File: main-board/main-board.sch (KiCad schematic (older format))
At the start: 114 parts, among them J1 BOOT, J10 8P8CDouble, J11 Qwiic, J12 Qwiic, J13 Qwiic, J14 YELLOW, J15 GREEN, J2 USB Header, J3 JTAG, J5 StatusPanel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

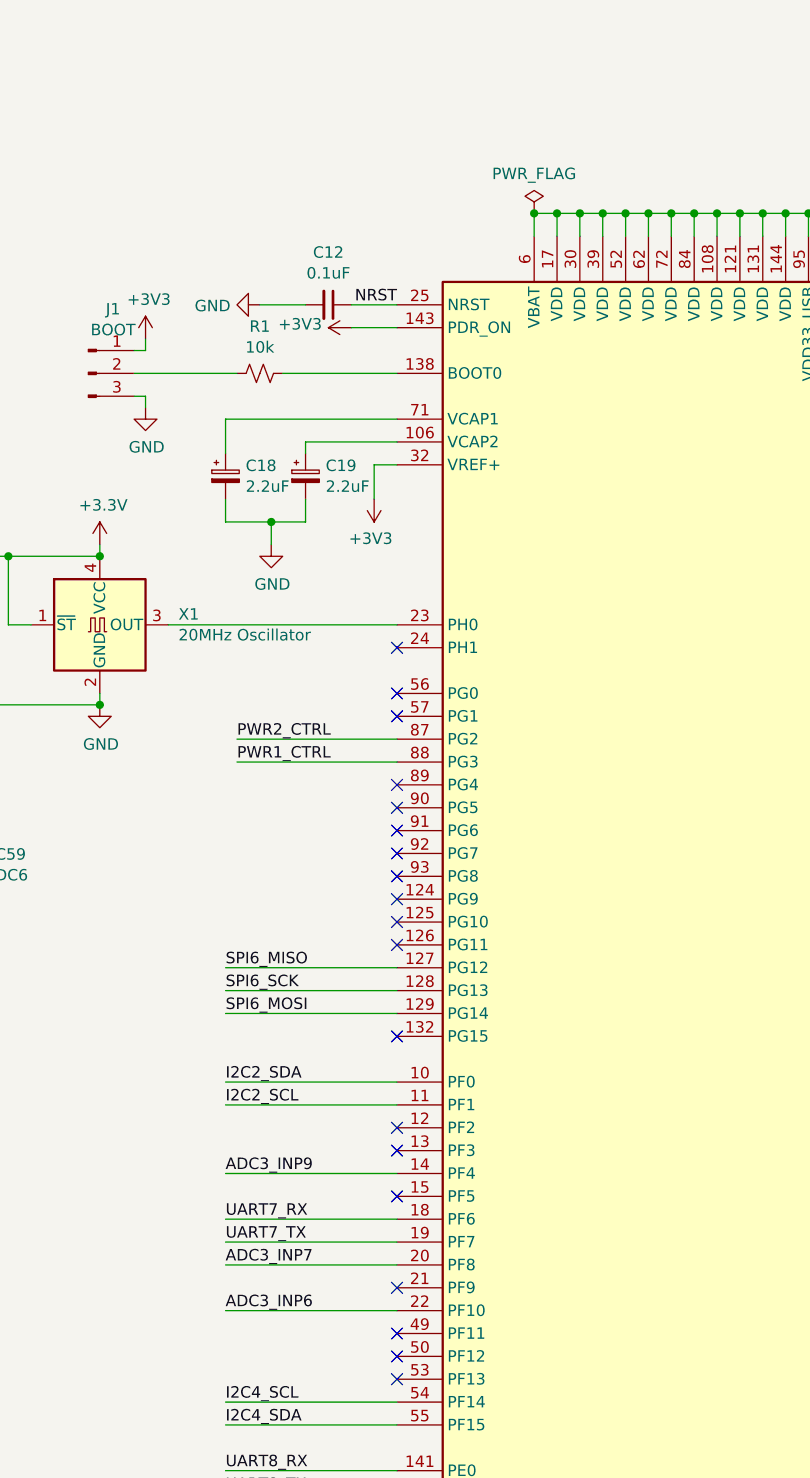
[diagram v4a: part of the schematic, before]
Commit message: Removed some unused nets and marked the pins NC
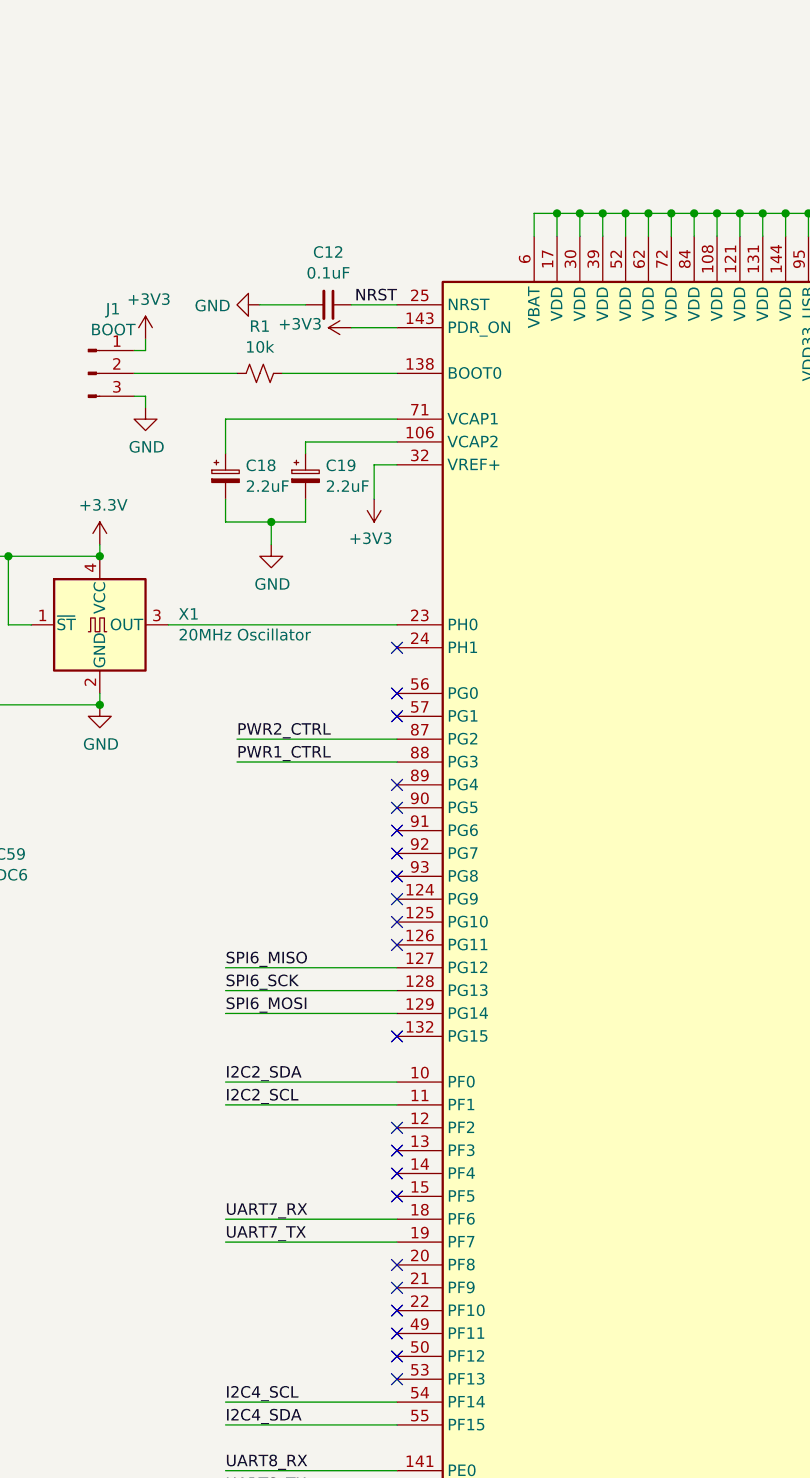
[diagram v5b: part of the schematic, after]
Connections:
- net ADC3_INP6: no longer names the net of U1.22 (PF10)
- net ADC3_INP7: no longer names the net of U1.20 (PF8)
- net ADC3_INP9: no longer names the net of U1.14 (PF4)
- no-connect marks 54 -> 57
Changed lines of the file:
@@
 USART1_RX
 Wire Wire Line
-	10650 6900 9900 6900
-Wire Wire Line
 	10650 7100 9900 7100
 Wire Wire Line
 	10650 7200 9900 7200
 Wire Wire Line
-	10650 7300 9900 7300
-Wire Wire Line
-	10650 7500 9900 7500
-Wire Wire Line
 	13150 6600 13850 6600
 Wire Wire Line
@@
 Text Label 13850 6600 2    50   ~ 0
 ETH_MDC
-Text Label 9900 6900 0    50   ~ 0
-ADC3_INP9
 Text Label 9900 7100 0    50   ~ 0
 UART7_RX
 Text Label 9900 7200 0    50   ~ 0
 UART7_TX
-Text Label 9900 7300 0    50   ~ 0
-ADC3_INP7
-Text Label 9900 7500 0    50   ~ 0
-ADC3_INP6
 Text Label 13900 3200 2    50   ~ 0
 ETH_RX_CLK
@@
 Connection ~ 12550 2700
 $Comp
-L power:PWR_FLAG #FLG0101
-U 1 1 628B99AF
-P 11250 2700
-F 0 "#FLG0101" H 11250 2775 50  0001 C CNN
-F 1 "PWR_FLAG" H 11250 2873 50  0000 C CNN
-F 2 "" H 11250 2700 50  0001 C CNN
-F 3 "~" H 11250 2700 50  0001 C CNN
-	1    11250 2700
-	1    0    0    -1
-$EndComp
-Connection ~ 11250 2700
-$Comp
 L ISL83490:ISL83490 U12
 U 1 1 62B08550
@@
 	1    0    0    -1
 $EndComp
+NoConn ~ 10650 7300
+NoConn ~ 10650 7500
+NoConn ~ 10650 6900
 $EndSCHEMATC

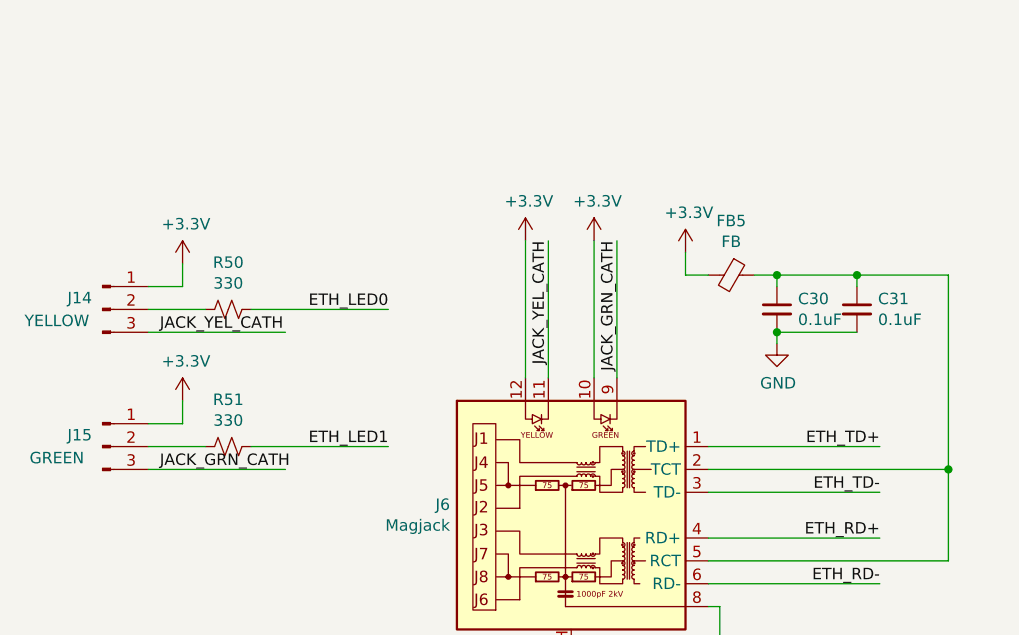
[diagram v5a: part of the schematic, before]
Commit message: Moved ethernet LEDs to a single 2x3 header instead of two 1x3
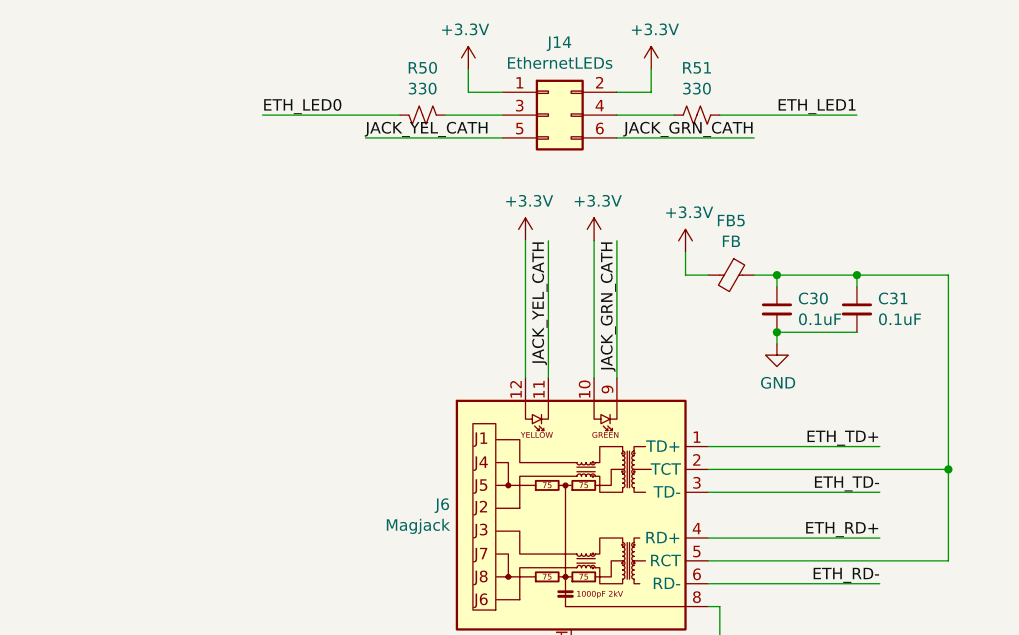
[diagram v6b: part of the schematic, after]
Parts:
- removed J14: YELLOW, Pin_Headers:Pin_Header_Straight_1x03_Pitch2.54mm, symbol Connector:Conn_01x03_Male
- removed J15: GREEN, Pin_Headers:Pin_Header_Straight_1x03_Pitch2.54mm, symbol Connector:Conn_01x03_Male
- added J14: EthernetLEDs, Pin_Headers:Pin_Header_Straight_2x03_Pitch2.54mm, symbol Connector_Generic:Conn_02x03_Odd_Even
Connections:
- net +3V3: now also J14.1 (Pin_1), J14.2 (Pin_2)
- net JACK_GRN_CATH: now also J14.6 (Pin_6)
- net JACK_YEL_CATH: now also J14.5 (Pin_5)
- net at R50.2: now also J14.3 (Pin_3)
- net at R51.2: now also J14.4 (Pin_4)
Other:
- moved on the sheet: R50, R51
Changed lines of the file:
@@
 JACK_GRN_CATH
-$Comp
-L Connector:Conn_01x03_Male J14
-U 1 1 602D7895
-P 850 1900
-F 0 "J14" H 750 1950 50  0000 C CNN
-F 1 "YELLOW" H 650 1850 50  0000 C CNN
-F 2 "Pin_Headers:Pin_Header_Straight_1x03_Pitch2.54mm" H 850 1900 50  0001 C CNN
-F 3 "~" H 850 1900 50  0001 C CNN
-	1    850  1900
-	1    0    0    -1
-$EndComp
-$Comp
-L Connector:Conn_01x03_Male J15
-U 1 1 602D90A8
-P 850 2500
-F 0 "J15" H 750 2550 50  0000 C CNN
-F 1 "GREEN" H 650 2450 50  0000 C CNN
-F 2 "Pin_Headers:Pin_Header_Straight_1x03_Pitch2.54mm" H 850 2500 50  0001 C CNN
-F 3 "~" H 850 2500 50  0001 C CNN
-	1    850  2500
-	1    0    0    -1
-$EndComp
 $Comp
 L power:+3.3V #PWR0187
 U 1 1 605E2E74
-P 1200 1700
-F 0 "#PWR0187" H 1200 1550 50  0001 C CNN
-F 1 "+3.3V" H 1215 1873 50  0000 C CNN
-F 2 "" H 1200 1700 50  0001 C CNN
-F 3 "" H 1200 1700 50  0001 C CNN
-	1    1200 1700
-	1    0    0    -1
+P 2450 850
+F 0 "#PWR0187" H 2450 700 50  0001 C CNN
+F 1 "+3.3V" H 2465 1023 50  0000 C CNN
+F 2 "" H 2450 850 50  0001 C CNN
+F 3 "" H 2450 850 50  0001 C CNN
+	1    2450 850
+	-1   0    0    -1
 $EndComp
 $Comp
@@
 $EndComp
 Wire Wire Line
-	1200 1700 1200 1800
-Wire Wire Line
-	1200 1800 1050 1800
-Wire Wire Line
-	1050 2000 1650 2000
-Text Label 1100 2000 0    50   ~ 0
+	2450 850  2450 950
+Wire Wire Line
+	2450 950  2600 950
+Wire Wire Line
+	2600 1150 2000 1150
+Text Label 2000 1150 0    50   ~ 0
 JACK_YEL_CATH
 Wire Wire Line
@@
 ETH_LED1
 Wire Wire Line
-	1050 2600 1650 2600
-Text Label 1100 2600 0    50   ~ 0
+	3100 1150 3700 1150
+Text Label 3700 1150 2    50   ~ 0
 JACK_GRN_CATH
 $Comp
 L power:+3.3V #PWR0190
 U 1 1 60BEFA4D
-P 1200 2300
-F 0 "#PWR0190" H 1200 2150 50  0001 C CNN
-F 1 "+3.3V" H 1215 2473 50  0000 C CNN
-F 2 "" H 1200 2300 50  0001 C CNN
-F 3 "" H 1200 2300 50  0001 C CNN
-	1    1200 2300
-	1    0    0    -1
-$EndComp
-Wire Wire Line
-	1200 2300 1200 2400
-Wire Wire Line
-	1200 2400 1050 2400
-Wire Wire Line
-	1500 2500 2100 2500
-Wire Wire Line
-	1500 1900 2100 1900
-Text Label 2100 1900 2    50   ~ 0
+P 3250 850
+F 0 "#PWR0190" H 3250 700 50  0001 C CNN
+F 1 "+3.3V" H 3265 1023 50  0000 C CNN
+F 2 "" H 3250 850 50  0001 C CNN
+F 3 "" H 3250 850 50  0001 C CNN
+	1    3250 850
+	1    0    0    -1
+$EndComp
+Wire Wire Line
+	3250 850  3250 950
+Wire Wire Line
+	3250 950  3100 950
+Wire Wire Line
+	3550 1050 4150 1050
+Wire Wire Line
+	2150 1050 1550 1050
+Text Label 1550 1050 0    50   ~ 0
 ETH_LED0
-Text Label 2100 2500 2    50   ~ 0
+Text Label 4150 1050 2    50   ~ 0
 ETH_LED1
 $Comp
 L Device:R_Small_US R50
 U 1 1 60F9F1DF
-P 1400 1900
-F 0 "R50" V 1195 1900 50  0000 C CNN
-F 1 "330" V 1286 1900 50  0000 C CNN
-F 2 "Resistors_SMD:R_0805" H 1400 1900 50  0001 C CNN
-F 3 "~" H 1400 1900 50  0001 C CNN
-	1    1400 1900
-	0    1    1    0
+P 2250 1050
+F 0 "R50" V 2045 1050 50  0000 C CNN
+F 1 "330" V 2136 1050 50  0000 C CNN
+F 2 "Resistors_SMD:R_0805" H 2250 1050 50  0001 C CNN
+F 3 "~" H 2250 1050 50  0001 C CNN
+	1    2250 1050
+	0    -1   1    0
 $EndComp
 $Comp
 L Device:R_Small_US R51
 U 1 1 60FA0ADB
-P 1400 2500
-F 0 "R51" V 1195 2500 50  0000 C CNN
-F 1 "330" V 1286 2500 50  0000 C CNN
-F 2 "Resistors_SMD:R_0805" H 1400 2500 50  0001 C CNN
-F 3 "~" H 1400 2500 50  0001 C CNN
-	1    1400 2500
+P 3450 1050
+F 0 "R51" V 3245 1050 50  0000 C CNN
+F 1 "330" V 3336 1050 50  0000 C CNN
+F 2 "Resistors_SMD:R_0805" H 3450 1050 50  0001 C CNN
+F 3 "~" H 3450 1050 50  0001 C CNN
+	1    3450 1050
 	0    1    1    0
 $EndComp
 Wire Wire Line
-	1050 1900 1300 1900
-Wire Wire Line
-	1050 2500 1300 2500
+	2600 1050 2350 1050
+Wire Wire Line
+	3100 1050 3350 1050
 Wire Wire Line
 	13150 9200 13850 9200
@@
 NoConn ~ 10650 7500
 NoConn ~ 10650 6900
+$Comp
+L Connector_Generic:Conn_02x03_Odd_Even J14
+U 1 1 61F985B2
+P 2800 1050
+F 0 "J14" H 2850 1367 50  0000 C CNN
+F 1 "EthernetLEDs" H 2850 1276 50  0000 C CNN
+F 2 "Pin_Headers:Pin_Header_Straight_2x03_Pitch2.54mm" H 2800 1050 50  0001 C CNN
+F 3 "~" H 2800 1050 50  0001 C CNN
+	1    2800 1050
+	1    0    0    -1
+$EndComp
 $EndSCHEMATC

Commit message: First round of rev 1 changes. This was a complete relayout.
* RS485 transceiver footprint fixed
* Compressed board to 100x100mm exactly
* Removed ethernet
* Changed FET footprints to SOT-23
* Swapped USB D+/D- to correct positions
* Spaced out +5V and GND silkscreen on power input
* Added JLCPCB order number silkscreen
* Spaced out Qwiic headers
* Added some more space around 3.3V regulator.
* Slightly increased size of electrolytic caps.
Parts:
- removed C21: 22uF, Capacitors_SMD:C_0805, symbol Device:C_Small
- removed C22, C23, C25, C26, C27, C28, C29, C30, C31, C32: 0.1uF, Capacitors_SMD:C_0805, symbol Device:C_Small
- removed C24: 1uF, Capacitors_SMD:C_0805, symbol Device:C_Small
- removed C45: DC, Capacitors_SMD:C_0805, symbol Device:C_Small
- removed C59: DC6, Capacitors_SMD:C_0805, symbol Device:C_Small
- removed FB3, FB4, FB5: FB, Inductors_SMD:L_0805, symbol Device:Ferrite_Bead_Small
- removed J14: EthernetLEDs, Pin_Headers:Pin_Header_Straight_2x03_Pitch2.54mm, symbol Connector_Generic:Conn_02x03_Odd_Even
- removed J6: Magjack, footprints:J1B1211111CCD, symbol Connector:Wuerth_7499010121A
- removed R50, R51: 330, Resistors_SMD:R_0805, symbol Device:R_Small_US
- removed U13: W25Q80DVSNIG, Housings_SOIC:SOIC-8_3.9x4.9mm_Pitch1.27mm, symbol Memory_Flash:MX25R3235FM1xx0
- removed U4: KSZ8041MLL, Housings_QFP:LQFP-48_7x7mm_Pitch0.5mm, symbol KSZ8041MLL:KSZ8041MLL
- removed X2: 25MHz Oscillator, Oscillators:Oscillator_SMD_SeikoEpson_SG8002CE-4pin_3.2x2.5mm_HandSoldering, symbol Oscillator:SG-5032CAN
- added J6: Qwiic, Connectors_JST:JST_SH_SM04B-SRSS-TB_04x1.00mm_Angled, symbol Connector:Conn_01x04_Female
- C20: value 22uF -> 1uF
- H1, H2, H3, H4: footprint Mounting_Holes:MountingHole_3.2mm_M3_Pad -> Mounting_Holes:MountingHole_3.2mm_M3_Pad_Via
- R6: value 0 -> 1200
- R7: value 6490 -> 1200
- U10, U11, U12, U5, U6, U7, U8, U9: footprint Housings_SOIC:SO-8_5.3x6.2mm_Pitch1.27mm -> Housings_SOIC:SOIC-8_3.9x4.9mm_Pitch1.27mm
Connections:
- net ETH_TXD3 is gone; now on net PWR8_CTRL: U1.1 (PE2)
- net +3V3: now also C20.1, FB2.1, R6.1, R7.1; no longer FB2.2, R6.2
- net D+: now also J2.3 (Pin_3), U2.1 (I/O1); no longer J2.4 (Pin_4), U2.3 (I/O2)
- net D-: now also J2.4 (Pin_4), U2.3 (I/O2); no longer J2.3 (Pin_3), U2.1 (I/O1)
- net GND: now also C20.2, J6.1 (Pin_1); no longer C20.1, R7.2
- net I2C1_SCL: now also J11.4 (Pin_4), R4.2; no longer J12.4 (Pin_4), R16.2
- net I2C1_SDA: now also J11.3 (Pin_3), R5.2; no longer J12.3 (Pin_3), R17.2
- net I2C2_SCL: now also R6.2, J6.4 (Pin_4); no longer J11.4 (Pin_4), R4.2
- net I2C2_SDA: now also R7.2, J6.3 (Pin_3); no longer J11.3 (Pin_3), R5.2
- net I2C4_SCL: now also J12.4 (Pin_4), R16.2; no longer J13.4 (Pin_4), R18.2
- net I2C4_SDA: now also J12.3 (Pin_3), R17.2; no longer J13.3 (Pin_3), R19.2
- net PWR1_CTRL: now also U1.86 (PD15); no longer U1.88 (PG3)
- net PWR2_CTRL: now also U1.88 (PG3); no longer U1.87 (PG2)
- net PWR4_CTRL: now also U1.87 (PG2); no longer U1.86 (PD15)
- net PWR5_CTRL: now also U1.4 (PE5); no longer U1.82 (PD13)
- net PWR6_CTRL: now also U1.2 (PE3); no longer U1.81 (PD12)
- net PWR7_CTRL: now also U1.3 (PE4); no longer U1.79 (PD10)
- net PWR8_CTRL: no longer U1.80 (PD11)
- net USB_D+: now also U2.6 (I/O1); no longer U2.4 (I/O2)
- net USB_D-: now also U2.4 (I/O2); no longer U2.6 (I/O1)
- net I2C3_SCL: now reaches U1.100 (PA8)
- net I2C3_SCL: now also J13.4 (Pin_4), R18.2
- net I2C3_SDA: now reaches U1.99 (PC9)
- net I2C3_SDA: now also J13.3 (Pin_3), R19.2
- net ETH_COL: no longer names the net of U1.37 (PA3)
- net ETH_CRS: no longer names the net of U1.34 (PA0)
- net ETH_INTRP: no longer names the net of U1.42 (PA6)
- net ETH_MDC: no longer names the net of U1.27 (PC1)
- net ETH_MDIO: no longer names the net of U1.36 (PA2)
- net ETH_RXD0: no longer names the net of U1.44 (PC4)
- net ETH_RXD1: no longer names the net of U1.45 (PC5)
- net ETH_RXD2: no longer names the net of U1.46 (PB0)
- net ETH_RXD3: no longer names the net of U1.47 (PB1)
- net ETH_RXER: no longer names the net of U1.41 (PA5)
- net ETH_RX_CLK: no longer names the net of U1.35 (PA1)
- net ETH_RX_DV: no longer names the net of U1.43 (PA7)
- net ETH_TXD0: no longer names the net of U1.73 (PB12)
- net ETH_TXD1: no longer names the net of U1.74 (PB13)
- net ETH_TXD2: no longer names the net of U1.28 (PC2_C)
- net ETH_TX_CLK: no longer names the net of U1.29 (PC3_C)
- net ETH_TX_EN: no longer names the net of U1.70 (PB11)
- new net: FB2.2, J6.2 (Pin_2)
- no-connect marks 57 -> 72

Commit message: MicroSD card slot and some IRQ headers.
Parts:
- added C21: DC, Capacitors_SMD:C_0805, symbol Device:C_Small
- added J14: Micro_SD_Card_Det, footprints:114-00841-68, symbol Connector:Micro_SD_Card_Det
- added J15: Interrupts1, Pin_Headers:Pin_Header_Straight_2x03_Pitch2.54mm, symbol Connector_Generic:Conn_02x03_Odd_Even
- added J16: Interrupts2, Pin_Headers:Pin_Header_Straight_2x03_Pitch2.54mm, symbol Connector_Generic:Conn_02x03_Odd_Even
- added R25: 10k, Resistors_SMD:R_0805, symbol Device:R_Small_US
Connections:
- net +3V3: now also C21.2, J14.4 (VDD), R25.1
- net GND: now also U1.66 (PE13), C21.1, J14.10 (DET_A), J14.6 (VSS), J15.2 (Pin_2), J15.4 (Pin_4), J15.6 (Pin_6), J16.2 (Pin_2), J16.4 (Pin_4), J16.6 (Pin_6)
- net SPI6_MISO: now also J14.7 (DAT0)
- net SPI6_MOSI: now also J14.3 (CMD)
- net SPI6_SCK: now also J14.5 (CLK)
- net SDCARD_CS: now reaches U1.46 (PB0)
- net SDCARD_CS: now also J14.2 (DAT3/CD)
- net QWIIC_EXTI10: now reaches U1.69 (PB10)
- net QWIIC_EXTI10: now also J15.1 (Pin_1), J16.5 (Pin_5)
- net QWIIC_EXTI11: now reaches U1.70 (PB11)
- net QWIIC_EXTI11: now also J15.3 (Pin_3), J15.5 (Pin_5)
- net QWIIC_EXTI12: now reaches U1.73 (PB12)
- net QWIIC_EXTI12: now also J16.3 (Pin_3)
- net QWIIC_EXTI13: now reaches U1.74 (PB13)
- net QWIIC_EXTI13: now also J16.1 (Pin_1)
- new net: J14.9 (DET_B), R25.2
- no-connect marks 72 -> 69
